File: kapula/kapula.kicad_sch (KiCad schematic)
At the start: 157 parts, among them J1 Conn_02x10_Odd_Even, J12 U.FL, J13 U.FL, J3 U.FL, J4 Conn_ARM_JTAG_SWD_10, J5 U.FL, J9 U.FL, Q1 AO3401A, Q1 BSS84, Q2 AO3401A, Q3 AO3400A, Q5 AO3400A, Q6 AO3400A, T1 BW21S7511A01TF, T2 BW21S7511A01TF, T3 BW21S7511A01TF, T4 BW21S7511A01TF, U1 XC6206P332MR, U2 TP4054, U3 DW01+G, U5 EFR32FG14P233F256GM48-B, U6 XA213-G4J, X1 DSB221SDN, Y1 32768 Hz

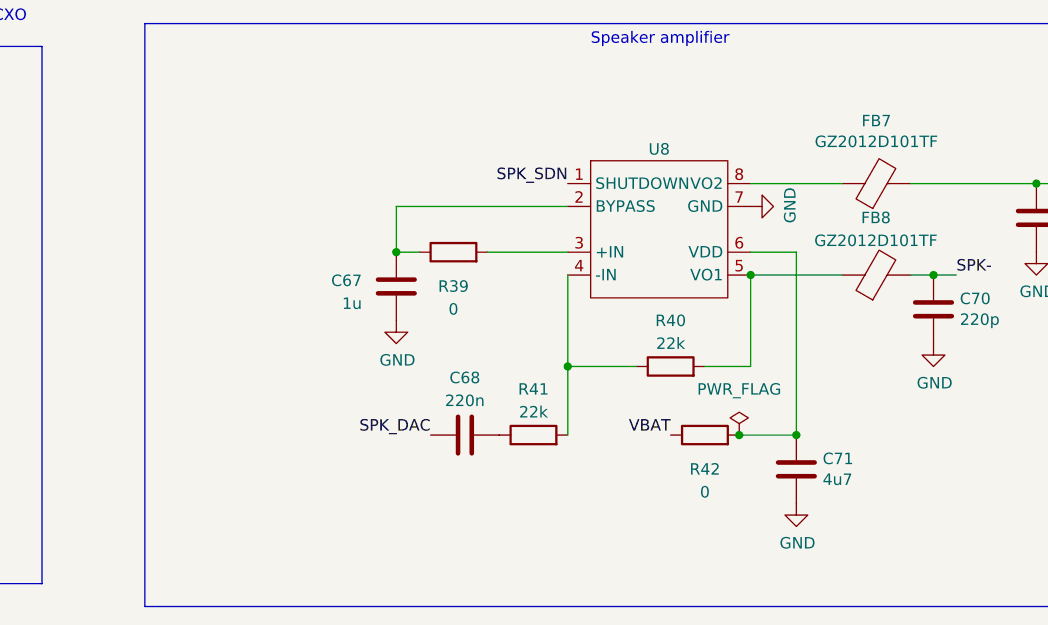
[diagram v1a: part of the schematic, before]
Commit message: Organize layout, a bit more routing
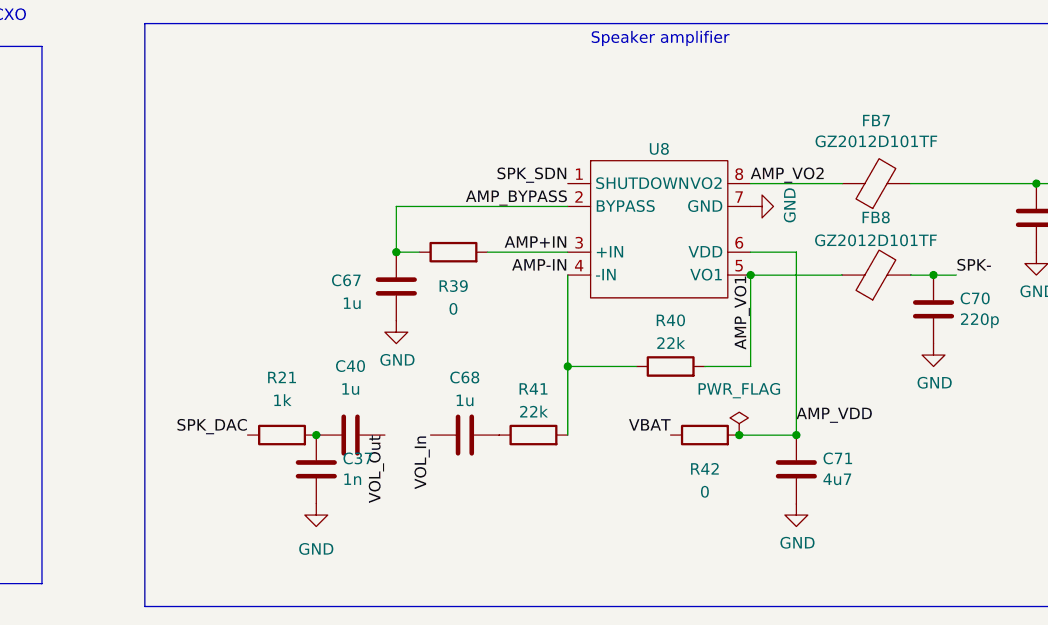
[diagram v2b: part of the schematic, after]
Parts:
- added C37: 1n, Capacitor_SMD:C_0402_1005Metric, symbol Device:C
- added C40: 1u, Capacitor_SMD:C_0603_1608Metric, symbol Device:C
- added R21: 1k, Resistor_SMD:R_0402_1005Metric, symbol Device:R
- C68: value 220n -> 1u; footprint Capacitor_SMD:C_0402_1005Metric -> Capacitor_SMD:C_0603_1608Metric; LCSC C16772 -> C15849
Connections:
- net GND: now also C37.2
- net SPK_DAC: now also R21.1; no longer C68.1
- net VOL_In: now also C68.1
- net VOL_Out: now also C40.2
- net AMP_VDD: now reaches C71.1, R42.2, U8.6 (VDD)
- net AMP_VO1: now reaches FB8.1, R40.2, U8.5 (VO1)
- net AMP_BYPASS: now reaches C67.1, R39.1, U8.2 (BYPASS)
- net AMP_VO2: now reaches FB7.1, U8.8 (VO2)
- net AMP+IN: now reaches R39.2, U8.3 (+IN)
- net AMP-IN: now reaches R40.1, R41.2, U8.4 (-IN)
- new net: C37.1, C40.1, R21.2
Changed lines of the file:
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@@
   (junction (at 128.27 168.91) (diameter 0) (color 0 0 0 0)
   )
+  (junction (at 162.56 261.62) (diameter 0) (color 0 0 0 0)
+  )
   (junction (at 109.22 64.77) (diameter 0) (color 0 0 0 0)
   )
@@
     (effects (font (size 1.27 1.27)) (justify right bottom))
   )
+  (label "VOL_Out" (at 170.18 261.62 270) (fields_autoplaced)
+    (effects (font (size 1.27 1.27)) (justify right bottom))
+  )
   (label "EFRin-" (at 163.83 134.62 0) (fields_autoplaced)
     (effects (font (size 1.27 1.27)) (justify left bottom))
@@
     (effects (font (size 1.27 1.27)) (justify left bottom))
   )
+  (label "AMP+IN" (at 190.5 241.3 180) (fields_autoplaced)
+    (effects (font (size 1.27 1.27)) (justify right bottom))
+  )
   (label "PF4" (at 133.35 154.94 270) (fields_autoplaced)
     (effects (font (size 1.27 1.27)) (justify right bottom))
@@
     (effects (font (size 1.27 1.27)) (justify right bottom))
   )
+  (label "AMP_VDD" (at 215.9 260.35 0) (fields_autoplaced)
+    (effects (font (size 1.27 1.27)) (justify left bottom))
+  )
   (label "PTT" (at 130.81 101.6 90) (fields_autoplaced)
     (effects (font (size 1.27 1.27)) (justify left bottom))
@@
     (effects (font (size 1.27 1.27)) (justify right bottom))
   )
+  (label "AMP-IN" (at 190.5 243.84 180) (fields_autoplaced)
+    (effects (font (size 1.27 1.27)) (justify right bottom))
+  )
   (label "VOL_In" (at 374.65 180.34 0) (fields_autoplaced)
     (effects (font (size 1.27 1.27)) (justify left bottom))
   )
+  (label "VOL_In" (at 175.26 261.62 270) (fields_autoplaced)
+    (effects (font (size 1.27 1.27)) (justify right bottom))
+  )
   (label "SWO_TDO" (at 452.12 240.03 0) (fields_autoplaced)
     (effects (font (size 1.27 1.27)) (justify left bottom))
@@
     (effects (font (size 1.27 1.27)) (justify right bottom))
   )
-  (label "SPK_DAC" (at 175.26 261.62 180) (fields_autoplaced)
+  (label "SPK_DAC" (at 154.94 261.62 180) (fields_autoplaced)
     (effects (font (size 1.27 1.27)) (justify right bottom))
   )
@@
     (effects (font (size 1.27 1.27)) (justify right bottom))
   )
+  (label "AMP_VO1" (at 210.82 243.84 270) (fields_autoplaced)
+    (effects (font (size 1.27 1.27)) (justify right bottom))
+  )
   (label "FILT_TRX" (at 339.09 142.24 90) (fields_autoplaced)
     (effects (font (size 1.27 1.27)) (justify left bottom))
@@
     (effects (font (size 1.27 1.27)) (justify left bottom))
   )
+  (label "AMP_BYPASS" (at 190.5 236.22 180) (fields_autoplaced)
+    (effects (font (size 1.27 1.27)) (justify right bottom))
+  )
   (label "PA0_TX" (at 334.01 232.41 0) (fields_autoplaced)
     (effects (font (size 1.27 1.27)) (justify left bottom))
@@
     (effects (font (size 1.27 1.27)) (justify right bottom))
   )
+  (label "AMP_VO2" (at 210.82 233.68 0) (fields_autoplaced)
+    (effects (font (size 1.27 1.27)) (justify left bottom))
+  )
   (label "VDD" (at 25.4 138.43 180) (fields_autoplaced)
     (effects (font (size 1.27 1.27)) (justify right bottom))
@@
     )
   )
+  (symbol (lib_id "Device:C") (at 162.56 265.43 0) (unit 1)
+    (in_bom yes) (on_board yes) (dnp no)
+    (property "Reference" "C37" (at 165.481 264.2616 0)
+      (effects (font (size 1.27 1.27)) (justify left))
+    )
+    (property "Value" "1n" (at 165.481 266.573 0)
+      (effects (font (size 1.27 1.27)) (justify left))
+    )
+    (property "Footprint" "Capacitor_SMD:C_0402_1005Metric" (at 163.5252 269.24 0)
+      (effects (font (size 1.27 1.27)) hide)
+    )
+    (property "Datasheet" "" (at 162.56 265.43 0)
+      (effects (font (size 1.27 1.27)) hide)
+    )
+    (property "LCSC" "C1523" (at 162.56 265.43 0)
+      (effects (font (size 1.27 1.27)) hide)
+    )
+    (pin "1")
+    (pin "2")
+    (instances
+      (project "kapula"
+        (path "/f2315993-072e-45c9-8c85-e79c6d40aba4"
+          (reference "C37") (unit 1)
+        )
+      )
+    )
+  )
   (symbol (lib_id "power:GND") (at 364.49 149.86 0) (unit 1)
     (in_bom yes) (on_board yes) (dnp no) (fields_autoplaced)
@@
       (effects (font (size 1.27 1.27)))
     )
-    (property "Value" "220n" (at 179.07 257.81 90)
+    (property "Value" "1u" (at 179.07 257.81 90)
       (effects (font (size 1.27 1.27)))
     )
-    (property "Footprint" "Capacitor_SMD:C_0402_1005Metric" (at 182.88 260.6548 0)
+    (property "Footprint" "Capacitor_SMD:C_0603_1608Metric" (at 182.88 260.6548 0)
       (effects (font (size 1.27 1.27)) hide)
     )
@@
       (effects (font (size 1.27 1.27)) hide)
     )
-    (property "LCSC" "C16772" (at 179.07 261.62 0)
+    (property "LCSC" "C15849" (at 179.07 261.62 0)
       (effects (font (size 1.27 1.27)) hide)
     )
@@
     )
   )
+  (symbol (lib_name "C_1") (lib_id "Device:C") (at 166.37 261.62 90) (unit 1)
+    (in_bom yes) (on_board yes) (dnp no) (fields_autoplaced)
+    (property "Reference" "C40" (at 166.37 254 90)
+      (effects (font (size 1.27 1.27)))
+    )
+    (property "Value" "1u" (at 166.37 256.54 90)
+      (effects (font (size 1.27 1.27)))
+    )
+    (property "Footprint" "Capacitor_SMD:C_0603_1608Metric" (at 170.18 260.6548 0)
+      (effects (font (size 1.27 1.27)) hide)
+    )
+    (property "Datasheet" "" (at 166.37 261.62 0)
+      (effects (font (size 1.27 1.27)) hide)
+    )
+    (property "LCSC" "C15849" (at 166.37 261.62 0)
+      (effects (font (size 1.27 1.27)) hide)
+    )
+    (pin "1")
+    (pin "2")
+    (instances
+      (project "kapula"
+        (path "/f2315993-072e-45c9-8c85-e79c6d40aba4"
+          (reference "C40") (unit 1)
+        )
+      )
+    )
+  )
   (symbol (lib_id "Transistor_FET:AO3400A") (at 195.58 -34.29 0) (mirror x) (unit 1)
     (in_bom yes) (on_board yes) (dnp no)
@@
     )
   )
+  (symbol (lib_id "Device:R") (at 158.75 261.62 90) (unit 1)
+    (in_bom yes) (on_board yes) (dnp no) (fields_autoplaced)
+    (property "Reference" "R21" (at 158.75 255.27 90)
+      (effects (font (size 1.27 1.27)))
+    )
+    (property "Value" "1k" (at 158.75 257.81 90)
+      (effects (font (size 1.27 1.27)))
+    )
+    (property "Footprint" "Resistor_SMD:R_0402_1005Metric" (at 158.75 263.398 90)
+      (effects (font (size 1.27 1.27)) hide)
+    )
+    (property "Datasheet" "" (at 158.75 261.62 0)
+      (effects (font (size 1.27 1.27)) hide)
+    )
+    (property "LCSC" "C11702" (at 158.75 261.62 0)
+      (effects (font (size 1.27 1.27)) hide)
+    )
+    (pin "1")
+    (pin "2")
+    (instances
+      (project "kapula"
+        (path "/f2315993-072e-45c9-8c85-e79c6d40aba4"
+          (reference "R21") (unit 1)
+        )
+      )
+    )
+  )
   (symbol (lib_id "Device:C") (at 212.09 127 270) (unit 1)
     (in_bom yes) (on_board yes) (dnp no) (fields_autoplaced)
@@
         )
       )
+    )
+  )
+  (symbol (lib_id "power:GND") (at 162.56 269.24 0) (unit 1)
+    (in_bom yes) (on_board yes) (dnp no) (fields_autoplaced)
+    (property "Reference" "#PWR052" (at 162.56 275.59 0)
+      (effects (font (size 1.27 1.27)) hide)
+    )
+    (property "Value" "GND" (at 162.56 274.32 0)
+      (effects (font (size 1.27 1.27)))
+    )
+    (property "Footprint" "" (at 162.56 269.24 0)
+      (effects (font (size 1.27 1.27)) hide)
+    )
+    (property "Datasheet" "" (at 162.56 269.24 0)
+      (effects (font (size 1.27 1.27)) hide)
+    )
+    (pin "1")
+    (instances
+      (project "kapula"
+        (path "/f2315993-072e-45c9-8c85-e79c6d40aba4"
+          (reference "#PWR052") (unit 1)
+        )
+      )
